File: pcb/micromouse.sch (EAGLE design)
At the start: 30 parts, among them J1 ENCODER_POLOLU, J2 ENCODER_POLOLU, Q1 PFET, U1 DRV8833PWP, U2 LD1117, U3 LM3480IM4

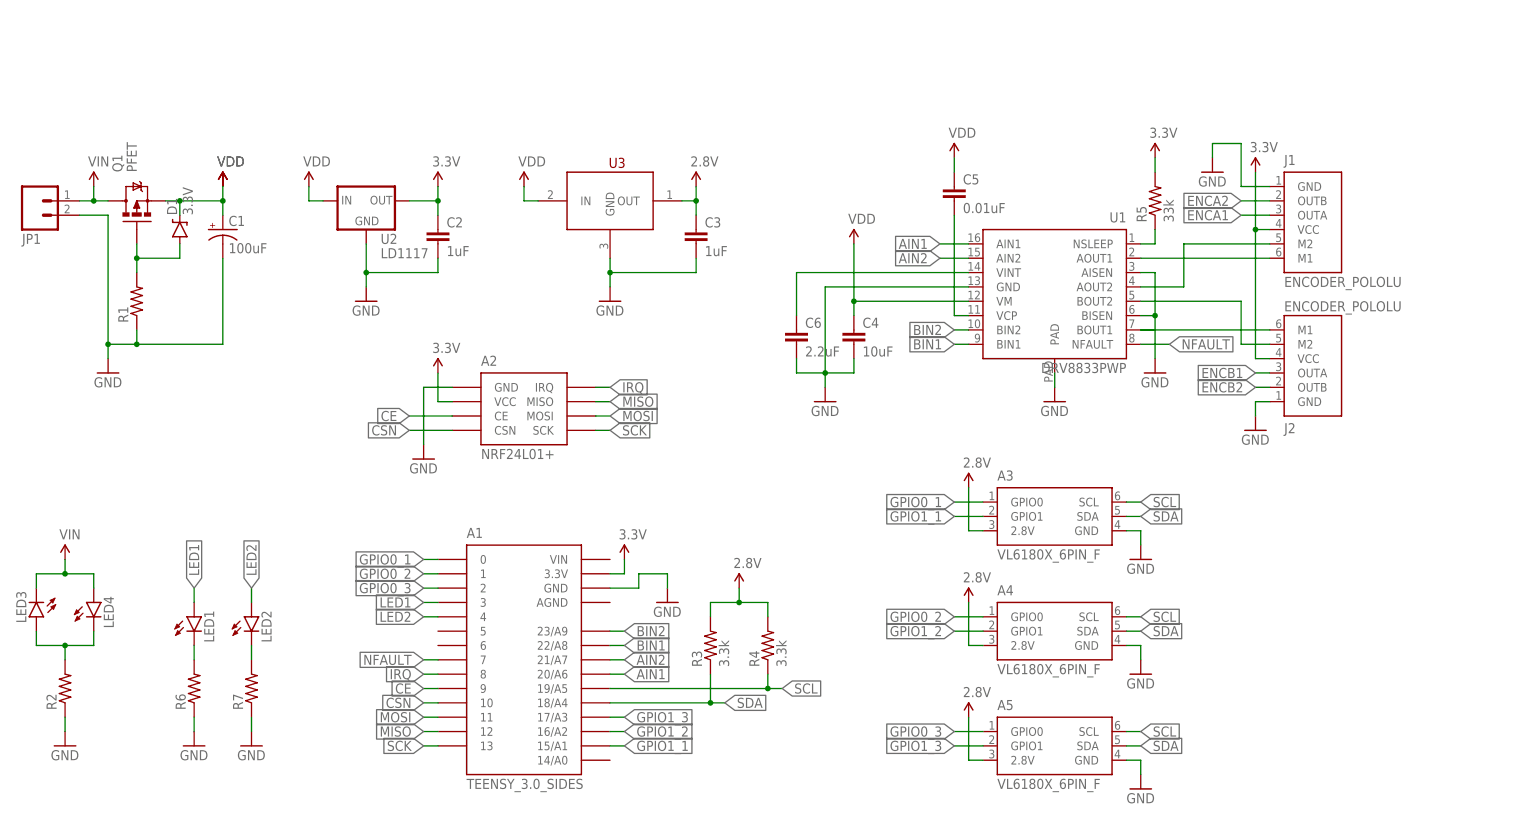
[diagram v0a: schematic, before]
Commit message: Added micromouse pcb layout
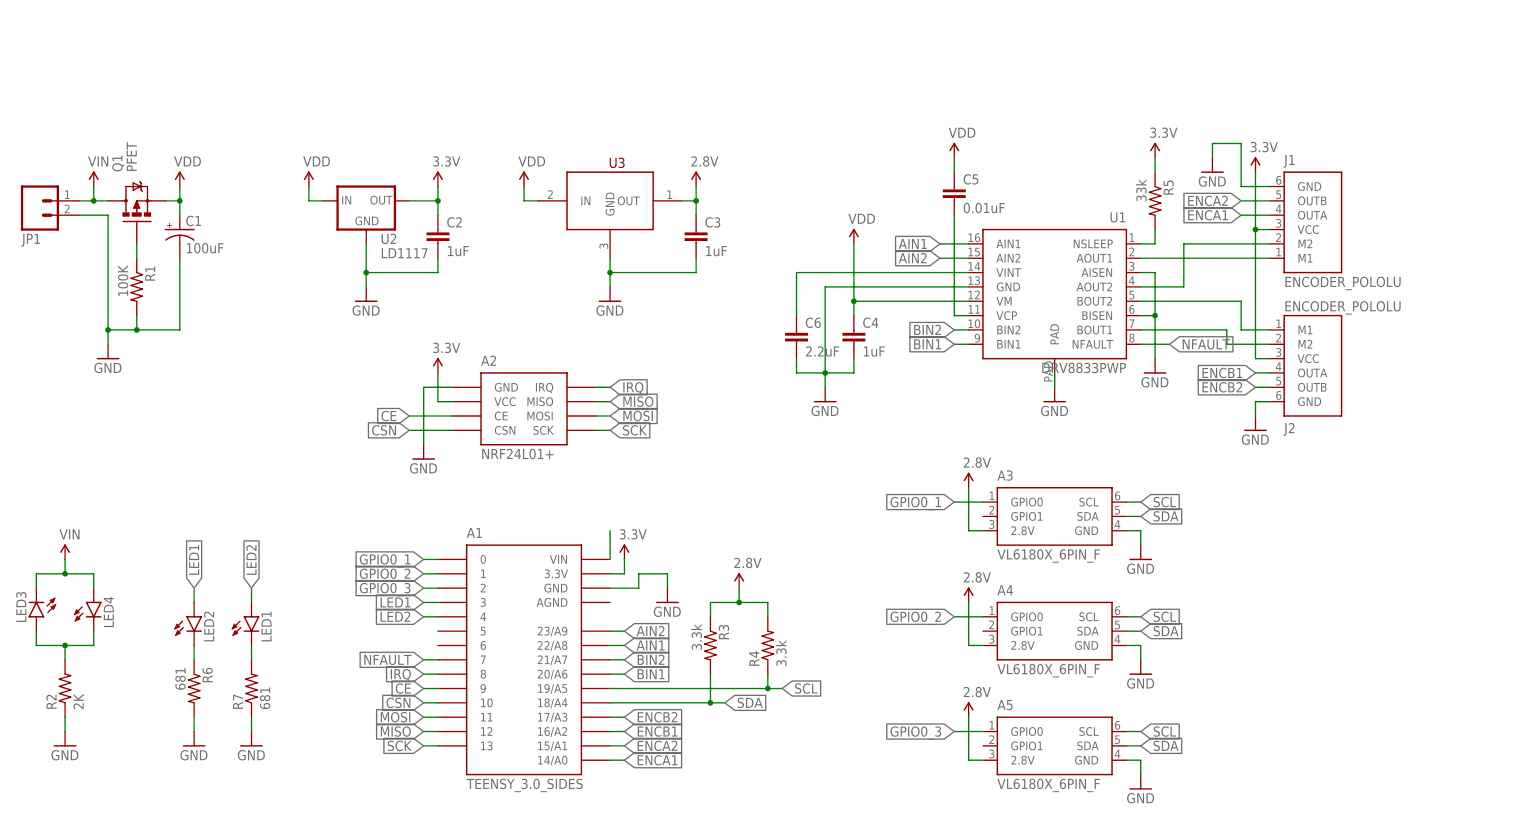
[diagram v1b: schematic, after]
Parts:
- removed D1: 3.3V, SparkFun-DiscreteSemi:DIODE-ZENER3.3V
- C4: value 10uF -> 1uF; device SparkFun-Capacitors:CAP1206 -> SparkFun-Capacitors:CAP0603-CAP
- R1: value (none) -> 100K
- R2: value (none) -> 2K
- R6, R7: value (none) -> 681
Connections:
- removed net GPIO1_1: A1.15/A1, A3.GPIO1
- removed net GPIO1_2: A1.16/A2, A4.GPIO1
- removed net GPIO1_3: A1.17/A3, A5.GPIO1
- removed net N$8: J2.M1, U1.BOUT1
- new net N$4: A1.VIN
- new net N$9: J2.M2, U1.BOUT1
- net 2.8V: now also R3.1; no longer R3.2
- net 3.3V: now also R5.1; no longer R5.2
- net AIN1: now also A1.22/A8; no longer A1.20/A6
- net AIN2: now also A1.23/A9; no longer A1.21/A7
- net BIN1: now also A1.20/A6; no longer A1.22/A8
- net BIN2: now also A1.21/A7; no longer A1.23/A9
- net ENCA1: now also A1.14/A0
- net ENCA2: now also A1.15/A1
- net ENCB1: now also A1.16/A2
- net ENCB2: now also A1.17/A3
- net GND: now also R1.2, R6.2; no longer R1.1, R6.1
- net LED1: now also LED2.A; no longer LED1.A
- net LED2: now also LED1.A; no longer LED2.A
- net N$1: now also R1.1; no longer D1.A, R1.2
- net N$10: now also R5.2; no longer R5.1
- net N$13: now also LED1.C; no longer LED2.C
- net N$5: now also LED2.C, R6.1; no longer LED1.C, R6.2
- net N$7: now also J2.M1; no longer J2.M2
- net SDA: now also R3.2; no longer R3.1
- net VDD: no longer D1.C
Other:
- moved on the sheet: C1, LED1, LED2, R1, R3, R5, R6

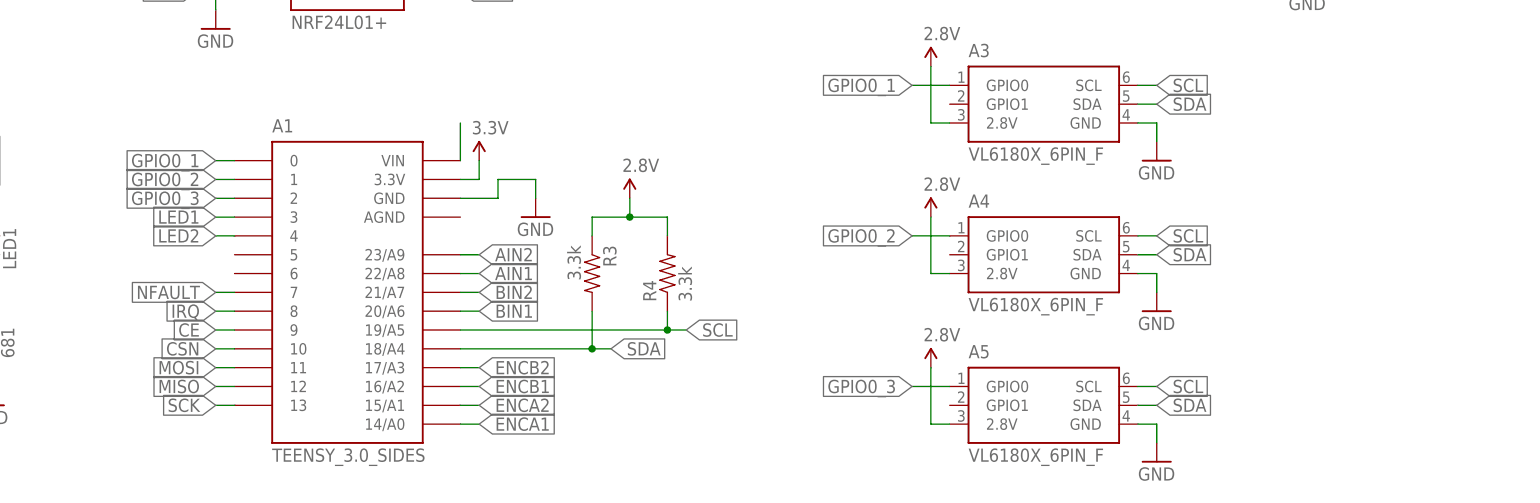
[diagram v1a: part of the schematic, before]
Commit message: Added buzzer
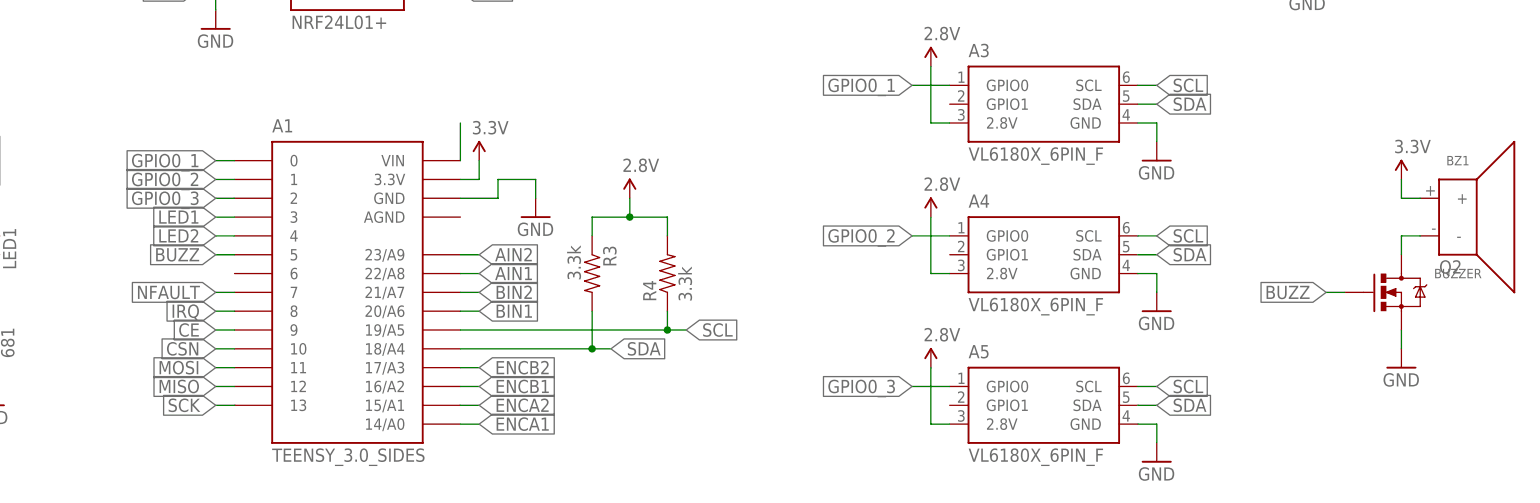
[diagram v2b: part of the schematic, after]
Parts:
- added BZ1: BUZZER, Custom:BUZZER
- added Q2: MOSFET-NCHANNELBSS123LT1G, SparkFun-DiscreteSemi:MOSFET-NCHANNELBSS123LT1G
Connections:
- new net BUZZ: A1.5, Q2.G
- new net N$8: BZ1.-, Q2.D
- net 3.3V: now also BZ1.+
- net GND: now also Q2.S
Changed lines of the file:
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@@
 <part name="GND16" library="SparkFun-Aesthetics" deviceset="GND" device=""/>
 <part name="C4" library="SparkFun-Capacitors" deviceset="CAP" device="0603-CAP" value="1uF"/>
+<part name="BZ1" library="Custom" deviceset="BUZZER" device=""/>
+<part name="SUPPLY5" library="SparkFun-Aesthetics" deviceset="3.3V" device=""/>
+<part name="Q2" library="SparkFun-DiscreteSemi" deviceset="MOSFET-NCHANNEL" device="BSS123LT1G" value=""/>
+<part name="GND17" library="SparkFun-Aesthetics" deviceset="GND" device=""/>
 </parts>
 <sheets>
@@
 <instance part="GND16" gate="1" x="43.18" y="10.16"/>
 <instance part="C4" gate="G$1" x="149.86" y="81.28"/>
+<instance part="BZ1" gate="G$1" x="241.3" y="35.56"/>
+<instance part="SUPPLY5" gate="G$1" x="233.68" y="40.64"/>
+<instance part="Q2" gate="G$1" x="233.68" y="25.4"/>
+<instance part="GND17" gate="1" x="233.68" y="15.24"/>
 </instances>
 <busses>
@@
 <wire x1="43.18" y1="12.7" x2="43.18" y2="15.24" width="0.1524" layer="91"/>
 </segment>
+<segment>
+<pinref part="Q2" gate="G$1" pin="S"/>
+<pinref part="GND17" gate="1" pin="GND"/>
+<wire x1="233.68" y1="17.78" x2="233.68" y2="20.32" width="0.1524" layer="91"/>
+</segment>
 </net>
 <net name="VDD" class="0">
@@
 <pinref part="A1" gate="G$1" pin="3.3V"/>
 <wire x1="106.68" y1="40.64" x2="109.22" y2="40.64" width="0.1524" layer="91"/>
+</segment>
+<segment>
+<pinref part="BZ1" gate="G$1" pin="+"/>
+<wire x1="236.22" y1="38.1" x2="233.68" y2="38.1" width="0.1524" layer="91"/>
+<wire x1="233.68" y1="38.1" x2="233.68" y2="40.64" width="0.1524" layer="91"/>
+<pinref part="SUPPLY5" gate="G$1" pin="3.3V"/>
 </segment>
 </net>
@@
 </segment>
 </net>
+<net name="N$8" class="0">
+<segment>
+<pinref part="BZ1" gate="G$1" pin="-"/>
+<pinref part="Q2" gate="G$1" pin="D"/>
+<wire x1="236.22" y1="33.02" x2="233.68" y2="33.02" width="0.1524" layer="91"/>
+<wire x1="233.68" y1="33.02" x2="233.68" y2="30.48" width="0.1524" layer="91"/>
+</segment>
+</net>
+<net name="BUZZ" class="0">
+<segment>
+<pinref part="A1" gate="G$1" pin="5"/>
+<wire x1="76.2" y1="30.48" x2="73.66" y2="30.48" width="0.1524" layer="91"/>
+<label x="73.66" y="30.48" size="1.778" layer="95" rot="R180" xref="yes"/>
+</segment>
+<segment>
+<pinref part="Q2" gate="G$1" pin="G"/>
+<wire x1="226.06" y1="25.4" x2="223.52" y2="25.4" width="0.1524" layer="91"/>
+<label x="223.52" y="25.4" size="1.778" layer="95" rot="R180" xref="yes"/>
+</segment>
+</net>

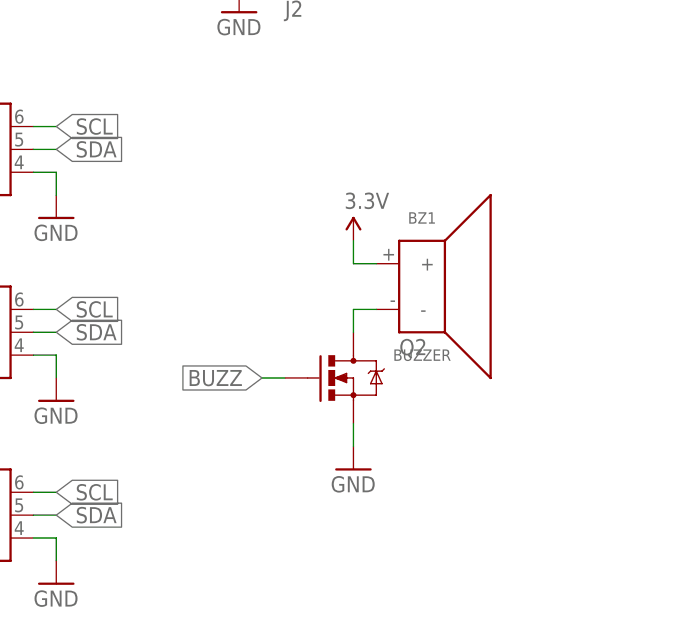
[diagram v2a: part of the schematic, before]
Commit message: Improved buzzer drive circuitry
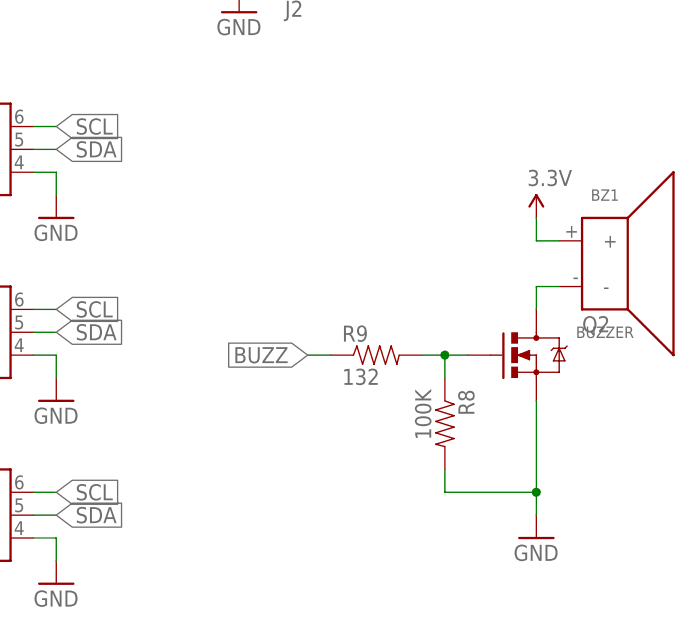
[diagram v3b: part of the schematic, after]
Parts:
- added R8: 100K, SparkFun-Resistors:RESISTOR0603
- added R9: 132, SparkFun-Resistors:RESISTOR0603
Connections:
- new net N$15: Q2.G, R8.1, R9.2
- net BUZZ: now also R9.1; no longer Q2.G
- net GND: now also R8.2
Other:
- moved on the sheet: BZ1, Q2
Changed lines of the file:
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@@
 <part name="Q2" library="SparkFun-DiscreteSemi" deviceset="MOSFET-NCHANNEL" device="BSS123LT1G" value=""/>
 <part name="GND17" library="SparkFun-Aesthetics" deviceset="GND" device=""/>
+<part name="R8" library="SparkFun-Resistors" deviceset="RESISTOR" device="0603" value="100K"/>
+<part name="R9" library="SparkFun-Resistors" deviceset="RESISTOR" device="0603" value="132"/>
 </parts>
 <sheets>
@@
 <instance part="GND16" gate="1" x="43.18" y="10.16"/>
 <instance part="C4" gate="G$1" x="149.86" y="81.28"/>
-<instance part="BZ1" gate="G$1" x="241.3" y="35.56"/>
-<instance part="SUPPLY5" gate="G$1" x="233.68" y="40.64"/>
-<instance part="Q2" gate="G$1" x="233.68" y="25.4"/>
-<instance part="GND17" gate="1" x="233.68" y="15.24"/>
+<instance part="BZ1" gate="G$1" x="261.62" y="38.1"/>
+<instance part="SUPPLY5" gate="G$1" x="254" y="43.18"/>
+<instance part="Q2" gate="G$1" x="254" y="27.94"/>
+<instance part="GND17" gate="1" x="254" y="7.62"/>
+<instance part="R8" gate="G$1" x="243.84" y="20.32" rot="R270"/>
+<instance part="R9" gate="G$1" x="236.22" y="27.94"/>
 </instances>
 <busses>
@@
 <pinref part="Q2" gate="G$1" pin="S"/>
 <pinref part="GND17" gate="1" pin="GND"/>
-<wire x1="233.68" y1="17.78" x2="233.68" y2="20.32" width="0.1524" layer="91"/>
+<wire x1="254" y1="10.16" x2="254" y2="12.7" width="0.1524" layer="91"/>
+<pinref part="R8" gate="G$1" pin="2"/>
+<wire x1="254" y1="12.7" x2="254" y2="22.86" width="0.1524" layer="91"/>
+<wire x1="243.84" y1="15.24" x2="243.84" y2="12.7" width="0.1524" layer="91"/>
+<wire x1="243.84" y1="12.7" x2="254" y2="12.7" width="0.1524" layer="91"/>
+<junction x="254" y="12.7"/>
 </segment>
 </net>
@@
 <segment>
 <pinref part="BZ1" gate="G$1" pin="+"/>
-<wire x1="236.22" y1="38.1" x2="233.68" y2="38.1" width="0.1524" layer="91"/>
-<wire x1="233.68" y1="38.1" x2="233.68" y2="40.64" width="0.1524" layer="91"/>
+<wire x1="256.54" y1="40.64" x2="254" y2="40.64" width="0.1524" layer="91"/>
+<wire x1="254" y1="40.64" x2="254" y2="43.18" width="0.1524" layer="91"/>
 <pinref part="SUPPLY5" gate="G$1" pin="3.3V"/>
 </segment>
@@
 <pinref part="BZ1" gate="G$1" pin="-"/>
 <pinref part="Q2" gate="G$1" pin="D"/>
-<wire x1="236.22" y1="33.02" x2="233.68" y2="33.02" width="0.1524" layer="91"/>
-<wire x1="233.68" y1="33.02" x2="233.68" y2="30.48" width="0.1524" layer="91"/>
+<wire x1="256.54" y1="35.56" x2="254" y2="35.56" width="0.1524" layer="91"/>
+<wire x1="254" y1="35.56" x2="254" y2="33.02" width="0.1524" layer="91"/>
 </segment>
 </net>
@@
 </segment>
 <segment>
+<pinref part="R9" gate="G$1" pin="1"/>
+<wire x1="231.14" y1="27.94" x2="228.6" y2="27.94" width="0.1524" layer="91"/>
+<label x="228.6" y="27.94" size="1.778" layer="95" rot="R180" xref="yes"/>
+</segment>
+</net>
+<net name="N$15" class="0">
+<segment>
 <pinref part="Q2" gate="G$1" pin="G"/>
-<wire x1="226.06" y1="25.4" x2="223.52" y2="25.4" width="0.1524" layer="91"/>
-<label x="223.52" y="25.4" size="1.778" layer="95" rot="R180" xref="yes"/>
-</segment>
-</net>
+<pinref part="R8" gate="G$1" pin="1"/>
+<wire x1="246.38" y1="27.94" x2="243.84" y2="27.94" width="0.1524" layer="91"/>
+<wire x1="243.84" y1="27.94" x2="243.84" y2="25.4" width="0.1524" layer="91"/>
+<wire x1="243.84" y1="27.94" x2="241.3" y2="27.94" width="0.1524" layer="91"/>
+<pinref part="R9" gate="G$1" pin="2"/>
+<junction x="243.84" y="27.94"/>
+</segment>
+</net>
